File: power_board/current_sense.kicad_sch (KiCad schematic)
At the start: 4 parts, among them U2 INA180A1

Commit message: Start multichannel layout
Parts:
- added C11: 100n, Capacitor_SMD:C_0603_1608Metric, symbol Device:C
- C12: renamed from C6; value C_Small -> 100n; footprint (none) -> Capacitor_SMD:C_0603_1608Metric
- R8: renamed from R7; footprint (none) -> Resistor_SMD:R_0603_1608Metric
- R9: renamed from R8; footprint (none) -> Resistor_SMD:R_0603_1608Metric
- renumbered U2 to U4
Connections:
- net +3V3A: now also C11.1
- net GNDA: now also C11.2
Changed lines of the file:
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@@
+	)
+	(junction
+		(at 73.66 44.45)
+		(diameter 0)
+		(color 0 0 0 0)
 	)
 	(junction
@@
 	(wire
 		(pts
+			(xy 73.66 44.45) (xy 73.66 57.15)
+		)
+		(stroke
+			(width 0)
+			(type default)
+		)
+	)
+	(wire
+		(pts
+			(xy 73.66 41.91) (xy 73.66 44.45)
+		)
+		(stroke
+			(width 0)
+			(type default)
+		)
+	)
+	(wire
+		(pts
 			(xy 50.8 67.31) (xy 68.58 67.31)
+		)
+		(stroke
+			(width 0)
+			(type default)
+		)
+	)
+	(wire
+		(pts
+			(xy 73.66 44.45) (xy 82.55 44.45)
 		)
 		(stroke
@@
 		(dnp no)
 		(fields_autoplaced yes)
-		(property "Reference" "R7"
+		(property "Reference" "R8"
 			(at 53.34 63.4999 0)
 			(effects
@@
 			)
 		)
-		(property "Footprint" ""
+		(property "Footprint" "Resistor_SMD:R_0603_1608Metric"
 			(at 50.8 64.77 0)
 			(effects
@@
 			(project ""
 				(path "/c786dd1f-c97f-4c1e-a27a-ac5828b3c50c/43aff6ba-bfeb-402e-8d33-59af370906e1"
-					(reference "R7")
+					(reference "R8")
 					(unit 1)
 				)
@@
 		(dnp no)
 		(fields_autoplaced yes)
-		(property "Reference" "R8"
+		(property "Reference" "R9"
 			(at 97.79 59.69 90)
 			(effects
@@
 			)
 		)
-		(property "Footprint" ""
+		(property "Footprint" "Resistor_SMD:R_0603_1608Metric"
 			(at 97.79 64.77 0)
 			(effects
@@
 			(project ""
 				(path "/c786dd1f-c97f-4c1e-a27a-ac5828b3c50c/43aff6ba-bfeb-402e-8d33-59af370906e1"
-					(reference "R8")
+					(reference "R9")
 					(unit 1)
 				)
@@
 		(dnp no)
 		(fields_autoplaced yes)
-		(property "Reference" "U2"
+		(property "Reference" "U4"
 			(at 87.63 58.3498 0)
 			(effects
@@
 			(project ""
 				(path "/c786dd1f-c97f-4c1e-a27a-ac5828b3c50c/43aff6ba-bfeb-402e-8d33-59af370906e1"
-					(reference "U2")
+					(reference "U4")
+					(unit 1)
+				)
+			)
+		)
+	)
+	(symbol
+		(lib_id "Device:C")
+		(at 82.55 48.26 0)
+		(unit 1)
+		(exclude_from_sim no)
+		(in_bom yes)
+		(on_board yes)
+		(dnp no)
+		(fields_autoplaced yes)
+		(property "Reference" "C11"
+			(at 86.36 46.9899 0)
+			(effects
+				(font
+					(size 1.27 1.27)
+				)
+				(justify left)
+			)
+		)
+		(property "Value" "100n"
+			(at 86.36 49.5299 0)
+			(effects
+				(font
+					(size 1.27 1.27)
+				)
+				(justify left)
+			)
+		)
+		(property "Footprint" "Capacitor_SMD:C_0603_1608Metric"
+			(at 83.5152 52.07 0)
+			(effects
+				(font
+					(size 1.27 1.27)
+				)
+				(hide yes)
+			)
+		)
+		(property "Datasheet" "~"
+			(at 82.55 48.26 0)
+			(effects
+				(font
+					(size 1.27 1.27)
+				)
+				(hide yes)
+			)
+		)
+		(property "Description" "Unpolarized capacitor"
+			(at 82.55 48.26 0)
+			(effects
+				(font
+					(size 1.27 1.27)
+				)
+				(hide yes)
+			)
+		)
+		(pin "2"
+		)
+		(pin "1"
+		)
+		(instances
+			(project ""
+				(path "/c786dd1f-c97f-4c1e-a27a-ac5828b3c50c/43aff6ba-bfeb-402e-8d33-59af370906e1"
+					(reference "C11")
 					(unit 1)
 				)
@@
 		(dnp no)
 		(fields_autoplaced yes)
-		(property "Reference" "#PWR032"
+		(property "Reference" "#PWR018"
 			(at 73.66 78.74 0)
 			(effects
@@
 			(project ""
 				(path "/c786dd1f-c97f-4c1e-a27a-ac5828b3c50c/43aff6ba-bfeb-402e-8d33-59af370906e1"
-					(reference "#PWR032")
+					(reference "#PWR018")
+					(unit 1)
+				)
+			)
+		)
+	)
+	(symbol
+		(lib_id "power:GNDA")
+		(at 82.55 52.07 0)
+		(unit 1)
+		(exclude_from_sim no)
+		(in_bom yes)
+		(on_board yes)
+		(dnp no)
+		(fields_autoplaced yes)
+		(property "Reference" "#PWR019"
+			(at 82.55 58.42 0)
+			(effects
+				(font
+					(size 1.27 1.27)
+				)
+				(hide yes)
+			)
+		)
+		(property "Value" "GNDA"
+			(at 82.55 57.15 0)
+			(effects
+				(font
+					(size 1.27 1.27)
+				)
+			)
+		)
+		(property "Footprint" ""
+			(at 82.55 52.07 0)
+			(effects
+				(font
+					(size 1.27 1.27)
+				)
+				(hide yes)
+			)
+		)
+		(property "Datasheet" ""
+			(at 82.55 52.07 0)
+			(effects
+				(font
+					(size 1.27 1.27)
+				)
+				(hide yes)
+			)
+		)
+		(property "Description" "Power symbol creates a global label with name \"GNDA\" , analog ground"
+			(at 82.55 52.07 0)
+			(effects
+				(font
+					(size 1.27 1.27)
+				)
+				(hide yes)
+			)
+		)
+		(pin "1"
+		)
+		(instances
+			(project "power_board"
+				(path "/c786dd1f-c97f-4c1e-a27a-ac5828b3c50c/43aff6ba-bfeb-402e-8d33-59af370906e1"
+					(reference "#PWR019")
 					(unit 1)
 				)
@@
 	(symbol
 		(lib_id "power:+3V3")
-		(at 73.66 57.15 0)
-		(unit 1)
-		(exclude_from_sim no)
-		(in_bom yes)
-		(on_board yes)
-		(dnp no)
-		(fields_autoplaced yes)
-		(property "Reference" "#PWR011"
-			(at 73.66 60.96 0)
+		(at 73.66 41.91 0)
+		(unit 1)
+		(exclude_from_sim no)
+		(in_bom yes)
+		(on_board yes)
+		(dnp no)
+		(fields_autoplaced yes)
+		(property "Reference" "#PWR017"
+			(at 73.66 45.72 0)
 			(effects
 				(font
@@
 		)
 		(property "Value" "+3V3A"
-			(at 73.66 52.07 0)
+			(at 73.66 36.83 0)
 			(effects
 				(font
@@
 		)
 		(property "Footprint" ""
-			(at 73.66 57.15 0)
+			(at 73.66 41.91 0)
 			(effects
 				(font
@@
 		)
 		(property "Datasheet" ""
-			(at 73.66 57.15 0)
+			(at 73.66 41.91 0)
 			(effects
 				(font
@@
 		)
 		(property "Description" "Power symbol creates a global label with name \"+3V3\""
-			(at 73.66 57.15 0)
+			(at 73.66 41.91 0)
 			(effects
 				(font
@@
 			(project "power_board"
 				(path "/c786dd1f-c97f-4c1e-a27a-ac5828b3c50c/43aff6ba-bfeb-402e-8d33-59af370906e1"
-					(reference "#PWR011")
+					(reference "#PWR017")
 					(unit 1)
 				)
@@
 		(dnp no)
 		(fields_autoplaced yes)
-		(property "Reference" "#PWR012"
+		(property "Reference" "#PWR020"
 			(at 102.87 78.74 0)
 			(effects
@@
 			(project "power_board"
 				(path "/c786dd1f-c97f-4c1e-a27a-ac5828b3c50c/43aff6ba-bfeb-402e-8d33-59af370906e1"
-					(reference "#PWR012")
+					(reference "#PWR020")
 					(unit 1)
 				)
@@
 		(dnp no)
 		(fields_autoplaced yes)
-		(property "Reference" "C6"
+		(property "Reference" "C12"
 			(at 105.41 66.0335 0)
 			(effects
@@
 			)
 		)
-		(property "Value" "C_Small"
+		(property "Value" "100n"
 			(at 105.41 68.5735 0)
 			(effects
@@
 			)
 		)
-		(property "Footprint" ""
+		(property "Footprint" "Capacitor_SMD:C_0603_1608Metric"
 			(at 102.87 67.31 0)
 			(effects
@@
 			(project ""
 				(path "/c786dd1f-c97f-4c1e-a27a-ac5828b3c50c/43aff6ba-bfeb-402e-8d33-59af370906e1"
-					(reference "C6")
-					(unit 1)
-				)
+					(reference "C12")
+					(unit 1)
+				)

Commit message: Complete primary layout step
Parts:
- removed R8: 0.001, Resistor_SMD:R_0603_1608Metric, symbol Device:R_Small
- added R8: HOVB4026-5W-0.5MR-1%, esc-library:RES-SMD_4P-L10.8-W6.7, symbol esc-library:HOVB4026-5W-0.5MR-1%
- renumbered C11 to C7, C12 to C8, U4 to U2
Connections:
- net current+: now also R8.2; no longer U2.3 (+)
- net current-: now also R8.1; no longer U2.4 (-)
- net +3V3A renamed +3V3A0
- new net: R8.4, U2.3 (+)
- new net: R8.3, U2.4 (-)
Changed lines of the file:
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@@
 		(color 0 0 0 0)
 	)
-	(junction
-		(at 50.8 67.31)
-		(diameter 0)
-		(color 0 0 0 0)
-	)
-	(junction
-		(at 50.8 62.23)
-		(diameter 0)
-		(color 0 0 0 0)
-	)
 	(wire
 		(pts
@@
 	(wire
 		(pts
+			(xy 43.18 57.15) (xy 43.18 59.69)
+		)
+		(stroke
+			(width 0)
+			(type default)
+		)
+	)
+	(wire
+		(pts
+			(xy 43.18 72.39) (xy 43.18 69.85)
+		)
+		(stroke
+			(width 0)
+			(type default)
+		)
+	)
+	(wire
+		(pts
 			(xy 95.25 64.77) (xy 83.82 64.77)
 		)
@@
 	(wire
 		(pts
-			(xy 50.8 67.31) (xy 68.58 67.31)
+			(xy 45.72 67.31) (xy 68.58 67.31)
 		)
 		(stroke
@@
 	(wire
 		(pts
-			(xy 45.72 62.23) (xy 50.8 62.23)
-		)
-		(stroke
-			(width 0)
-			(type default)
-		)
-	)
-	(wire
-		(pts
 			(xy 102.87 64.77) (xy 111.76 64.77)
 		)
@@
 	(wire
 		(pts
-			(xy 50.8 62.23) (xy 68.58 62.23)
-		)
-		(stroke
-			(width 0)
-			(type default)
-		)
-	)
-	(wire
-		(pts
-			(xy 45.72 67.31) (xy 50.8 67.31)
+			(xy 45.72 62.23) (xy 68.58 62.23)
 		)
 		(stroke
@@
 			(width 0)
 			(type default)
+		)
+	)
+	(hierarchical_label "current+"
+		(shape input)
+		(at 43.18 57.15 180)
+		(effects
+			(font
+				(size 1.27 1.27)
+			)
+			(justify right)
 		)
 	)
 	(hierarchical_label "current-"
 		(shape input)
-		(at 45.72 67.31 180)
+		(at 43.18 72.39 180)
 		(effects
 			(font
@@
 		)
 	)
-	(hierarchical_label "current+"
-		(shape input)
-		(at 45.72 62.23 180)
-		(effects
-			(font
-				(size 1.27 1.27)
-			)
-			(justify right)
-		)
-	)
-	(symbol
-		(lib_id "Device:R_Small")
-		(at 50.8 64.77 0)
-		(unit 1)
-		(exclude_from_sim no)
-		(in_bom yes)
-		(on_board yes)
-		(dnp no)
-		(fields_autoplaced yes)
-		(property "Reference" "R8"
-			(at 53.34 63.4999 0)
-			(effects
-				(font
-					(size 1.016 1.016)
-				)
-				(justify left)
-			)
-		)
-		(property "Value" "0.001"
-			(at 53.34 66.0399 0)
-			(effects
-				(font
-					(size 1.27 1.27)
-				)
-				(justify left)
-			)
-		)
-		(property "Footprint" "Resistor_SMD:R_0603_1608Metric"
-			(at 50.8 64.77 0)
-			(effects
-				(font
-					(size 1.27 1.27)
-				)
-				(hide yes)
-			)
-		)
-		(property "Datasheet" "~"
-			(at 50.8 64.77 0)
-			(effects
-				(font
-					(size 1.27 1.27)
-				)
-				(hide yes)
-			)
-		)
-		(property "Description" "Resistor, small symbol"
-			(at 50.8 64.77 0)
-			(effects
-				(font
-					(size 1.27 1.27)
-				)
-				(hide yes)
-			)
-		)
-		(pin "1"
-		)
-		(pin "2"
-		)
-		(instances
-			(project ""
-				(path "/c786dd1f-c97f-4c1e-a27a-ac5828b3c50c/43aff6ba-bfeb-402e-8d33-59af370906e1"
-					(reference "R8")
-					(unit 1)
-				)
-			)
-		)
-	)
 	(symbol
 		(lib_id "Device:R_Small")
@@
 		(dnp no)
 		(fields_autoplaced yes)
-		(property "Reference" "U4"
+		(property "Reference" "U2"
 			(at 87.63 58.3498 0)
 			(effects
@@
 			(project ""
 				(path "/c786dd1f-c97f-4c1e-a27a-ac5828b3c50c/43aff6ba-bfeb-402e-8d33-59af370906e1"
-					(reference "U4")
+					(reference "U2")
 					(unit 1)
 				)
@@
 		(dnp no)
 		(fields_autoplaced yes)
-		(property "Reference" "C11"
+		(property "Reference" "C7"
 			(at 86.36 46.9899 0)
 			(effects
@@
 			(project ""
 				(path "/c786dd1f-c97f-4c1e-a27a-ac5828b3c50c/43aff6ba-bfeb-402e-8d33-59af370906e1"
-					(reference "C11")
+					(reference "C7")
 					(unit 1)
 				)
@@
 		(dnp no)
 		(fields_autoplaced yes)
-		(property "Reference" "#PWR018"
+		(property "Reference" "#PWR026"
 			(at 73.66 78.74 0)
 			(effects
@@
 			(project ""
 				(path "/c786dd1f-c97f-4c1e-a27a-ac5828b3c50c/43aff6ba-bfeb-402e-8d33-59af370906e1"
-					(reference "#PWR018")
+					(reference "#PWR026")
+					(unit 1)
+				)
+			)
+		)
+	)
+	(symbol
+		(lib_id "power:+3V3")
+		(at 73.66 41.91 0)
+		(unit 1)
+		(exclude_from_sim no)
+		(in_bom yes)
+		(on_board yes)
+		(dnp no)
+		(fields_autoplaced yes)
+		(property "Reference" "#PWR025"
+			(at 73.66 45.72 0)
+			(effects
+				(font
+					(size 1.27 1.27)
+				)
+				(hide yes)
+			)
+		)
+		(property "Value" "+3V3A0"
+			(at 73.66 36.83 0)
+			(effects
+				(font
+					(size 1.27 1.27)
+				)
+			)
+		)
+		(property "Footprint" ""
+			(at 73.66 41.91 0)
+			(effects
+				(font
+					(size 1.27 1.27)
+				)
+				(hide yes)
+			)
+		)
+		(property "Datasheet" ""
+			(at 73.66 41.91 0)
+			(effects
+				(font
+					(size 1.27 1.27)
+				)
+				(hide yes)
+			)
+		)
+		(property "Description" "Power symbol creates a global label with name \"+3V3\""
+			(at 73.66 41.91 0)
+			(effects
+				(font
+					(size 1.27 1.27)
+				)
+				(hide yes)
+			)
+		)
+		(pin "1"
+		)
+		(instances
+			(project "power_board"
+				(path "/c786dd1f-c97f-4c1e-a27a-ac5828b3c50c/43aff6ba-bfeb-402e-8d33-59af370906e1"
+					(reference "#PWR025")
 					(unit 1)
 				)
@@
 		(dnp no)
 		(fields_autoplaced yes)
-		(property "Reference" "#PWR019"
+		(property "Reference" "#PWR027"
 			(at 82.55 58.42 0)
 			(effects
@@
 			(project "power_board"
 				(path "/c786dd1f-c97f-4c1e-a27a-ac5828b3c50c/43aff6ba-bfeb-402e-8d33-59af370906e1"
-					(reference "#PWR019")
-					(unit 1)
-				)
-			)
-		)
-	)
-	(symbol
-		(lib_id "power:+3V3")
-		(at 73.66 41.91 0)
-		(unit 1)
-		(exclude_from_sim no)
-		(in_bom yes)
-		(on_board yes)
-		(dnp no)
-		(fields_autoplaced yes)
-		(property "Reference" "#PWR017"
-			(at 73.66 45.72 0)
-			(effects
-				(font
-					(size 1.27 1.27)
-				)
-				(hide yes)
-			)
-		)
-		(property "Value" "+3V3A"
-			(at 73.66 36.83 0)
-			(effects
-				(font
-					(size 1.27 1.27)
-				)
-			)
-		)
-		(property "Footprint" ""
-			(at 73.66 41.91 0)
-			(effects
-				(font
-					(size 1.27 1.27)
-				)
-				(hide yes)
-			)
-		)
-		(property "Datasheet" ""
-			(at 73.66 41.91 0)
-			(effects
-				(font
-					(size 1.27 1.27)
-				)
-				(hide yes)
-			)
-		)
-		(property "Description" "Power symbol creates a global label with name \"+3V3\""
-			(at 73.66 41.91 0)
-			(effects
-				(font
-					(size 1.27 1.27)
-				)
-				(hide yes)
-			)
-		)
-		(pin "1"
-		)
-		(instances
-			(project "power_board"
-				(path "/c786dd1f-c97f-4c1e-a27a-ac5828b3c50c/43aff6ba-bfeb-402e-8d33-59af370906e1"
-					(reference "#PWR017")
+					(reference "#PWR027")
+					(unit 1)
+				)
+			)
+		)
+	)
+	(symbol
+		(lib_id "esc-library:HOVB4026-5W-0.5MR-1%")
+		(at 43.18 64.77 90)
+		(unit 1)
+		(exclude_from_sim no)
+		(in_bom yes)
+		(on_board yes)
+		(dnp no)
+		(fields_autoplaced yes)
+		(property "Reference" "R8"
+			(at 40.64 63.4999 90)
+			(effects
+				(font
+					(size 1.27 1.27)
+				)
+				(justify left)
+			)
+		)
+		(property "Value" "HOVB4026-5W-0.5MR-1%"
+			(at 40.64 66.0399 90)
+			(effects
+				(font
+					(size 1.27 1.27)
+				)
+				(justify left)
+			)
+		)
+		(property "Footprint" "esc-library:RES-SMD_4P-L10.8-W6.7"
+			(at 53.34 64.77 0)
+			(effects
+				(font
+					(size 1.27 1.27)
+				)
+				(hide yes)
+			)
+		)
+		(property "Datasheet" "https://lcsc.com/product-detail/Low-Resistors-Current-Sense-Resistors-Surface-Mount_Milliohm-HOVB4026-5W-0-5mR-1_C481533.html"
+			(at 55.88 64.77 0)
+			(effects
+				(font
+					(size 1.27 1.27)
+				)
+				(hide yes)
+			)
+		)
+		(property "Description" ""
+			(at 43.18 64.77 0)
+			(effects
+				(font
+					(size 1.27 1.27)
+				)
+				(hide yes)
+			)
+		)
+		(property "LCSC Part" "C481533"
+			(at 58.42 64.77 0)
+			(effects
+				(font
+					(size 1.27 1.27)
+				)
+				(hide yes)
+			)
+		)
+		(pin "3"
+		)
+		(pin "4"
+		)
+		(pin "2"
+		)
+		(pin "1"
+		)
+		(instances
+			(project ""
+				(path "/c786dd1f-c97f-4c1e-a27a-ac5828b3c50c/43aff6ba-bfeb-402e-8d33-59af370906e1"
+					(reference "R8")
 					(unit 1)
 				)
@@
 		(dnp no)
 		(fields_autoplaced yes)
-		(property "Reference" "#PWR020"
+		(property "Reference" "#PWR028"
 			(at 102.87 78.74 0)
 			(effects
@@
 			(project "power_board"
 				(path "/c786dd1f-c97f-4c1e-a27a-ac5828b3c50c/43aff6ba-bfeb-402e-8d33-59af370906e1"
-					(reference "#PWR020")
+					(reference "#PWR028")
 					(unit 1)
 				)
@@
 		(dnp no)
 		(fields_autoplaced yes)
-		(property "Reference" "C12"
+		(property "Reference" "C8"
 			(at 105.41 66.0335 0)
 			(effects
@@
 			(project ""
 				(path "/c786dd1f-c97f-4c1e-a27a-ac5828b3c50c/43aff6ba-bfeb-402e-8d33-59af370906e1"
-					(reference "C12")
-					(unit 1)
-				)
+					(reference "C8")
+					(unit 1)
+				)

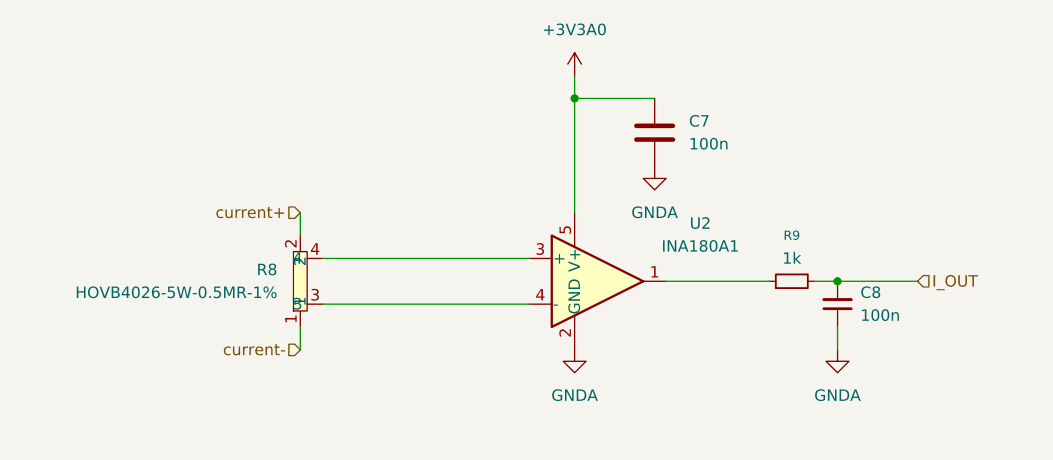
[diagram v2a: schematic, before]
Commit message: Add testpoint, SWD, and PWM port
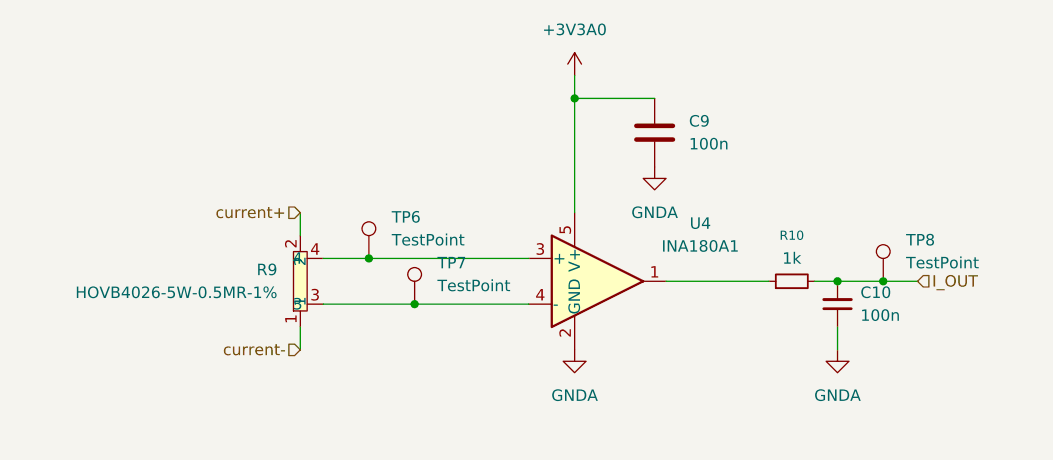
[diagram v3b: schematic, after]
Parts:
- added TP6, TP7, TP8: TestPoint, esc-library:SMD_RH-5015, symbol Connector:TestPoint
- renumbered C8 to C10, C7 to C9, R9 to R10, R8 to R9, U2 to U4
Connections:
- net I_OUT: now also TP8.1
- net at R9.4, U4.3 (+): now also TP6.1
- net at R9.3, U4.4 (-): now also TP7.1

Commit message: Complete all design, pass DRC
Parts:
- added TP35: GND, esc-library:SMD_RH-5015, symbol Connector:TestPoint
- TP6: value TestPoint -> SHUNT_P
- TP7: value TestPoint -> SHUNT_N
- TP8: value TestPoint -> I_SENSE
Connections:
- new net GND: TP35.1
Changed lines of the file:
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@@
+	(symbol
+		(lib_id "Connector:TestPoint")
+		(at 116.84 76.2 0)
+		(unit 1)
+		(exclude_from_sim no)
+		(in_bom yes)
+		(on_board yes)
+		(dnp no)
+		(fields_autoplaced yes)
+		(property "Reference" "TP35"
+			(at 119.38 71.6279 0)
+			(effects
+				(font
+					(size 1.27 1.27)
+				)
+				(justify left)
+			)
+		)
+		(property "Value" "GND"
+			(at 119.38 74.1679 0)
+			(effects
+				(font
+					(size 1.27 1.27)
+				)
+				(justify left)
+			)
+		)
+		(property "Footprint" "esc-library:SMD_RH-5015"
+			(at 121.92 76.2 0)
+			(effects
+				(font
+					(size 1.27 1.27)
+				)
+				(hide yes)
+			)
+		)
+		(property "Datasheet" "~"
+			(at 121.92 76.2 0)
+			(effects
+				(font
+					(size 1.27 1.27)
+				)
+				(hide yes)
+			)
+		)
+		(property "Description" "test point"
+			(at 116.84 76.2 0)
+			(effects
+				(font
+					(size 1.27 1.27)
+				)
+				(hide yes)
+			)
+		)
+		(pin "1"
+		)
+		(instances
+			(project "power_board"
+				(path "/c786dd1f-c97f-4c1e-a27a-ac5828b3c50c/43aff6ba-bfeb-402e-8d33-59af370906e1"
+					(reference "TP35")
+					(unit 1)
+				)
+			)
+		)
+	)
 	(symbol
 		(lib_id "Connector:TestPoint")
@@
 			)
 		)
-		(property "Value" "TestPoint"
+		(property "Value" "SHUNT_N"
 			(at 58.42 65.2779 0)
 			(effects
@@
 			)
 		)
-		(property "Value" "TestPoint"
+		(property "Value" "I_SENSE"
 			(at 110.49 62.7379 0)
 			(effects
@@
 	)
 	(symbol
+		(lib_id "power:GND")
+		(at 116.84 76.2 0)
+		(unit 1)
+		(exclude_from_sim no)
+		(in_bom yes)
+		(on_board yes)
+		(dnp no)
+		(fields_autoplaced yes)
+		(property "Reference" "#PWR064"
+			(at 116.84 82.55 0)
+			(effects
+				(font
+					(size 1.27 1.27)
+				)
+				(hide yes)
+			)
+		)
+		(property "Value" "GND"
+			(at 116.84 81.28 0)
+			(effects
+				(font
+					(size 1.27 1.27)
+				)
+			)
+		)
+		(property "Footprint" ""
+			(at 116.84 76.2 0)
+			(effects
+				(font
+					(size 1.27 1.27)
+				)
+				(hide yes)
+			)
+		)
+		(property "Datasheet" ""
+			(at 116.84 76.2 0)
+			(effects
+				(font
+					(size 1.27 1.27)
+				)
+				(hide yes)
+			)
+		)
+		(property "Description" "Power symbol creates a global label with name \"GND\" , ground"
+			(at 116.84 76.2 0)
+			(effects
+				(font
+					(size 1.27 1.27)
+				)
+				(hide yes)
+			)
+		)
+		(pin "1"
+		)
+		(instances
+			(project "power_board"
+				(path "/c786dd1f-c97f-4c1e-a27a-ac5828b3c50c/43aff6ba-bfeb-402e-8d33-59af370906e1"
+					(reference "#PWR064")
+					(unit 1)
+				)
+			)
+		)
+	)
+	(symbol
 		(lib_id "power:+3V3")
 		(at 73.66 41.91 0)
@@
 			)
 		)
-		(property "Value" "TestPoint"
+		(property "Value" "SHUNT_P"
 			(at 53.34 60.1979 0)
 			(effects
